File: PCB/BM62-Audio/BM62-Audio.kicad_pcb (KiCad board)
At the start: 2 copper layers, 3 parts, among them J1 AudioJack3, J2 USB_C_Receptacle_USB2.0

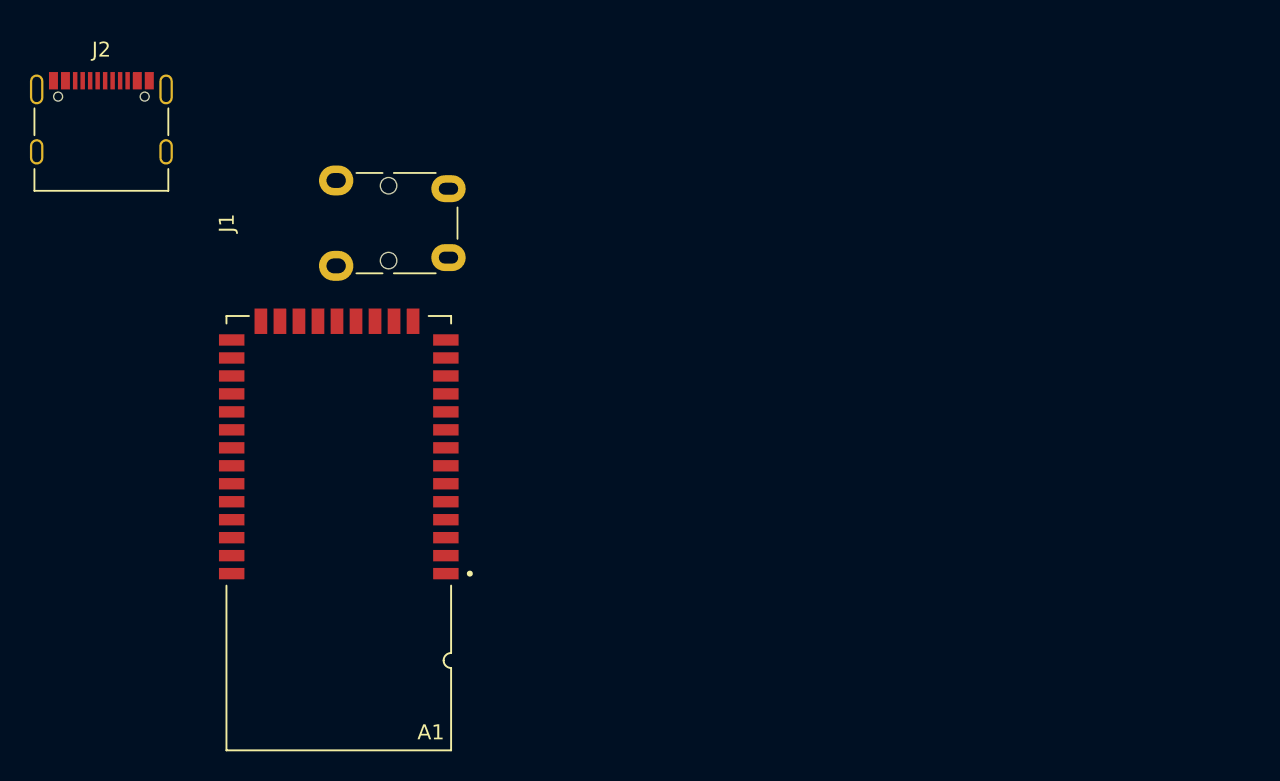
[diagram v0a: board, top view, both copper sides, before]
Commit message: ✏️ 回路図の基礎ができた
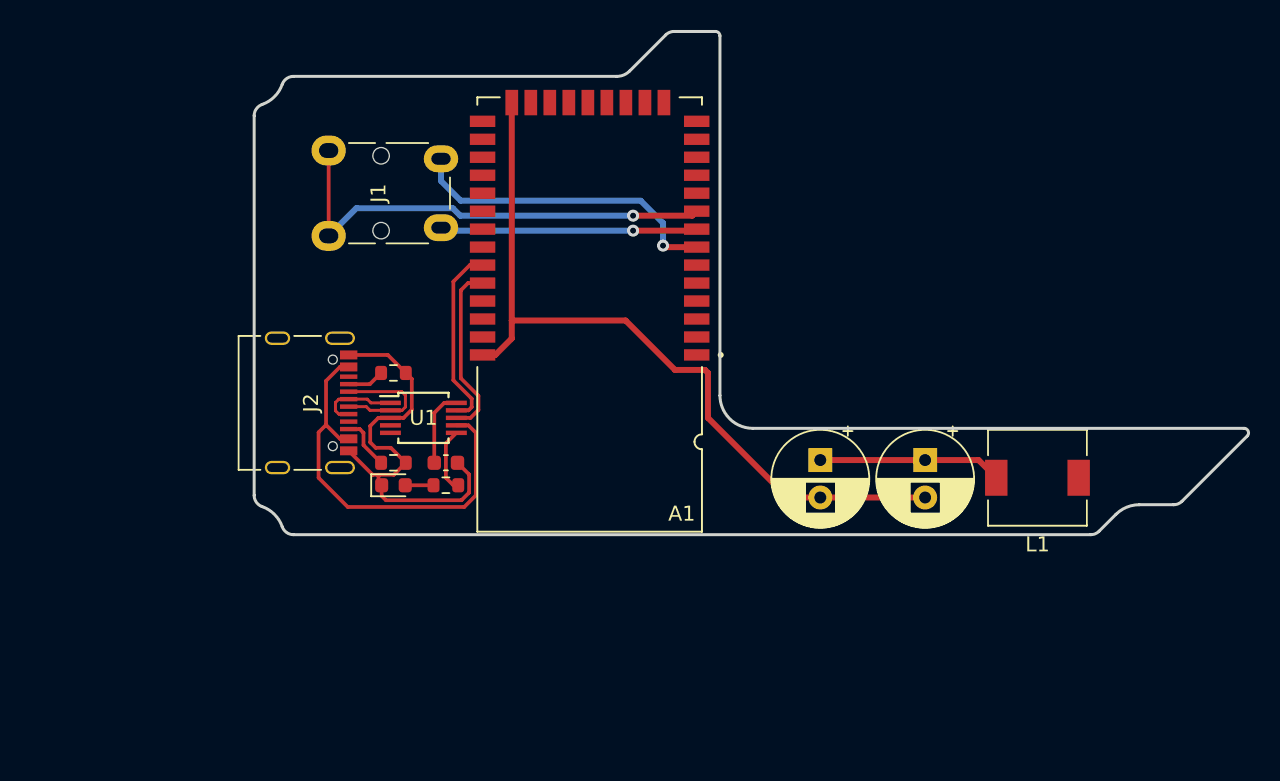
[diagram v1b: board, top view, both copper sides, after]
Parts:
- added C1: 0.1µ, Capacitor_SMD:C_0603_1608Metric, F.Cu at (85.0, 83.0)
- added C2: 100µ, Capacitor_THT:CP_Radial_D6.3mm_P2.50mm, F.Cu at (117.0, 82.8)
- added C3: 100µ, Capacitor_THT:CP_Radial_D6.3mm_P2.50mm, F.Cu at (110.0, 82.8)
- added D1: WHITE, LED_SMD:LED_0603_1608Metric, F.Cu at (81.5, 84.5)
- added L1: 47µ, Inductor_SMD:L_6.3x6.3_H3, F.Cu at (124.5, 84.0)
- added R1: 5.1k, Resistor_SMD:R_0603_1608Metric, F.Cu at (81.5, 77.0)
- added R2: 5.1k, Resistor_SMD:R_0603_1608Metric, F.Cu at (81.5, 83.0)
- added R3: 1k, Resistor_SMD:R_0603_1608Metric, F.Cu at (85.0, 84.5)
- added U1: CH340E, Package_SO:MSOP-10_3x3mm_P0.5mm, F.Cu at (83.5, 80.0)
- moved J2 23.6 mm to (76.0, 79.0), turned to -90 degrees
- moved A1 22.2 mm to (102.1, 58.6)
- moved J1 2.06 mm to (77.2, 67.8)
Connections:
- net Net-(J2-VBUS-PadA4) renamed +5V
- A1 pad 23: unconnected-(A1-GND-Pad23) -> GND
- A1 pad 24: unconnected-(A1-SYS_PWR-Pad24) -> /SYS PWR OUT
- A1 pad 26: unconnected-(A1-MFB-Pad26) -> /FUNC BUTTON
- A1 pad 27: unconnected-(A1-LED1-Pad27) -> /LED1
- A1 pad 28: unconnected-(A1-LED2-Pad28) -> /LED2
- A1 pad 32: unconnected-(A1-HCI_TXD-Pad32) -> /USB-RX BM62-TX
- A1 pad 33: unconnected-(A1-HCI_RXD-Pad33) -> /USB-TX BM62-RX
- A1 pad 37: unconnected-(A1-GND__1-Pad37) -> GND
- A1 pad 7: unconnected-(A1-SPKR-Pad7) -> /AUDIO OUT Rch
- A1 pad 8: unconnected-(A1-AOHPM-Pad8) -> /AUDIO OUT COM
- A1 pad 9: unconnected-(A1-SPKL-Pad9) -> /AUDIO OUT Lch
- J1 pad R: unconnected-(J1-PadR) -> /AUDIO OUT Rch
- J1 pad S: unconnected-(J1-PadS) -> /AUDIO OUT COM
- J1 pad T: unconnected-(J1-PadT) -> /AUDIO OUT Lch
- J2 pad A1: Net-(J2-GND-PadA1) -> GND
- J2 pad A12: Net-(J2-GND-PadA1) -> GND
- J2 pad A5: unconnected-(J2-CC1-PadA5) -> Net-(J2-CC1)
- J2 pad A6: unconnected-(J2-D+-PadA6) -> /D+
- J2 pad A7: unconnected-(J2-D--PadA7) -> /D-
- J2 pad B1: Net-(J2-GND-PadA1) -> GND
- J2 pad B12: Net-(J2-GND-PadA1) -> GND
- J2 pad B5: unconnected-(J2-CC2-PadB5) -> Net-(J2-CC2)
- J2 pad B6: unconnected-(J2-D+-PadB6) -> /D+
- J2 pad B7: unconnected-(J2-D--PadB7) -> /D-
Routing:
- net GND: track 0.00 -> 81.4 mm
- net /AUDIO OUT Lch: track 0.00 -> 31.4 mm, vias 0 -> 1
- net +5V: track 0.00 -> 27.8 mm
- net /AUDIO OUT Rch: track 0.00 -> 21.3 mm, vias 0 -> 1
- net /AUDIO OUT COM: track 0.00 -> 17.2 mm, vias 0 -> 1
- net /USB-RX BM62-TX: track 0.00 -> 12.4 mm
- net Net-(C2-Pad1): track 0.00 -> 12.2 mm
- net /USB-TX BM62-RX: track 0.00 -> 11.8 mm
- net /D-: track 0.00 -> 8.65 mm
- net /D+: track 0.00 -> 5.39 mm
- net Net-(U1-V3): track 0.00 -> 5.09 mm
- net Net-(U1-TNOW): track 0.00 -> 4.32 mm
- net Net-(J2-CC2): track 0.00 -> 3.58 mm
- net Net-(J2-CC1): track 0.00 -> 2.48 mm
- net Net-(D1-A): track 0.00 -> 1.89 mm
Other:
- board outline added: 66.4 x 33.6 mm
